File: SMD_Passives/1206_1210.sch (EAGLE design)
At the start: 4 parts

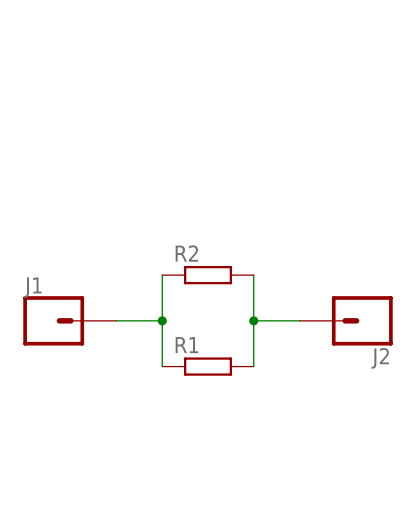
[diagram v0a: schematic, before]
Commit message: Updated passive SMD breakout boards to meet PCB specs
JLC PCB requires a 5x5mm minimum size, and the single SMD adapters were too small for this, so converted to make them wide enough, and made them "dual" to maximize the spaced used
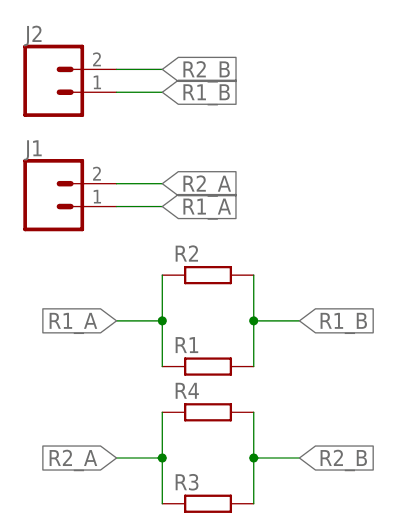
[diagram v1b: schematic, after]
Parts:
- added R3: (no value), bschulz_passives:R-EU_R1210
- added R4: (no value), bschulz_passives:R-EU_R1206
- J1, J2: device bschulz:CONN_01 -> bschulz:CONN_02
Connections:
- net N$1 renamed R1_A
- net N$2 renamed R1_B
- new net R2_A: J1.2, R3.1, R4.1
- new net R2_B: J2.2, R3.2, R4.2
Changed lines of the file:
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@@
 <part name="R1" library="bschulz_passives" deviceset="R-EU_" device="R1210"/>
 <part name="R2" library="bschulz_passives" deviceset="R-EU_" device="R1206"/>
-<part name="J1" library="bschulz" deviceset="CONN_01" device="" package3d_urn="urn:adsk.eagle:package:38028/1"/>
-<part name="J2" library="bschulz" deviceset="CONN_01" device="" package3d_urn="urn:adsk.eagle:package:38028/1"/>
+<part name="J1" library="bschulz" deviceset="CONN_02" device=""/>
+<part name="J2" library="bschulz" deviceset="CONN_02" device=""/>
+<part name="R3" library="bschulz_passives" deviceset="R-EU_" device="R1210"/>
+<part name="R4" library="bschulz_passives" deviceset="R-EU_" device="R1206"/>
 </parts>
 <sheets>
@@
 <attribute name="VALUE" x="21.59" y="14.478" size="1.778" layer="96"/>
 </instance>
-<instance part="J1" gate="G$1" x="7.62" y="12.7" smashed="yes">
-<attribute name="VALUE" x="5.08" y="7.874" size="1.778" layer="96" font="vector"/>
-<attribute name="NAME" x="5.08" y="15.748" size="1.778" layer="95" font="vector"/>
+<instance part="J1" gate="G$1" x="7.62" y="25.4" smashed="yes">
+<attribute name="VALUE" x="5.08" y="20.574" size="1.778" layer="96" font="vector"/>
+<attribute name="NAME" x="5.08" y="30.988" size="1.778" layer="95" font="vector"/>
 </instance>
-<instance part="J2" gate="G$1" x="43.18" y="12.7" smashed="yes" rot="R180">
-<attribute name="VALUE" x="45.72" y="17.526" size="1.778" layer="96" font="vector" rot="R180"/>
-<attribute name="NAME" x="45.72" y="9.652" size="1.778" layer="95" font="vector" rot="R180"/>
+<instance part="J2" gate="G$1" x="7.62" y="38.1" smashed="yes">
+<attribute name="VALUE" x="5.08" y="33.274" size="1.778" layer="96" font="vector"/>
+<attribute name="NAME" x="5.08" y="43.688" size="1.778" layer="95" font="vector"/>
+</instance>
+<instance part="R3" gate="G$1" x="25.4" y="-7.62" smashed="yes">
+<attribute name="NAME" x="21.59" y="-6.1214" size="1.778" layer="95"/>
+<attribute name="VALUE" x="21.59" y="-10.922" size="1.778" layer="96"/>
+</instance>
+<instance part="R4" gate="G$1" x="25.4" y="2.54" smashed="yes">
+<attribute name="NAME" x="21.59" y="4.0386" size="1.778" layer="95"/>
+<attribute name="VALUE" x="21.59" y="-0.762" size="1.778" layer="96"/>
 </instance>
 </instances>
@@
 </busses>
 <nets>
-<net name="N$1" class="0">
+<net name="R2_B" class="0">
+<segment>
+<pinref part="J2" gate="G$1" pin="2"/>
+<wire x1="15.24" y1="40.64" x2="20.32" y2="40.64" width="0.1524" layer="91"/>
+<label x="20.32" y="40.64" size="1.778" layer="95" xref="yes"/>
+</segment>
+<segment>
+<pinref part="R4" gate="G$1" pin="2"/>
+<pinref part="R3" gate="G$1" pin="2"/>
+<wire x1="30.48" y1="2.54" x2="30.48" y2="-2.54" width="0.1524" layer="91"/>
+<wire x1="30.48" y1="-2.54" x2="30.48" y2="-7.62" width="0.1524" layer="91"/>
+<wire x1="35.56" y1="-2.54" x2="30.48" y2="-2.54" width="0.1524" layer="91"/>
+<junction x="30.48" y="-2.54"/>
+<label x="35.56" y="-2.54" size="1.778" layer="95" xref="yes"/>
+</segment>
+</net>
+<net name="R1_B" class="0">
+<segment>
+<pinref part="J2" gate="G$1" pin="1"/>
+<wire x1="15.24" y1="38.1" x2="20.32" y2="38.1" width="0.1524" layer="91"/>
+<label x="20.32" y="38.1" size="1.778" layer="95" xref="yes"/>
+</segment>
+<segment>
+<pinref part="R2" gate="G$1" pin="2"/>
+<pinref part="R1" gate="G$1" pin="2"/>
+<wire x1="30.48" y1="17.78" x2="30.48" y2="12.7" width="0.1524" layer="91"/>
+<wire x1="30.48" y1="12.7" x2="30.48" y2="7.62" width="0.1524" layer="91"/>
+<wire x1="35.56" y1="12.7" x2="30.48" y2="12.7" width="0.1524" layer="91"/>
+<junction x="30.48" y="12.7"/>
+<label x="35.56" y="12.7" size="1.778" layer="95" xref="yes"/>
+</segment>
+</net>
+<net name="R2_A" class="0">
+<segment>
+<pinref part="J1" gate="G$1" pin="2"/>
+<wire x1="15.24" y1="27.94" x2="20.32" y2="27.94" width="0.1524" layer="91"/>
+<label x="20.32" y="27.94" size="1.778" layer="95" xref="yes"/>
+</segment>
+<segment>
+<pinref part="R3" gate="G$1" pin="1"/>
+<pinref part="R4" gate="G$1" pin="1"/>
+<wire x1="20.32" y1="-7.62" x2="20.32" y2="-2.54" width="0.1524" layer="91"/>
+<wire x1="20.32" y1="-2.54" x2="20.32" y2="2.54" width="0.1524" layer="91"/>
+<wire x1="15.24" y1="-2.54" x2="20.32" y2="-2.54" width="0.1524" layer="91"/>
+<junction x="20.32" y="-2.54"/>
+<label x="15.24" y="-2.54" size="1.778" layer="95" rot="R180" xref="yes"/>
+</segment>
+</net>
+<net name="R1_A" class="0">
+<segment>
+<pinref part="J1" gate="G$1" pin="1"/>
+<wire x1="15.24" y1="25.4" x2="20.32" y2="25.4" width="0.1524" layer="91"/>
+<label x="20.32" y="25.4" size="1.778" layer="95" xref="yes"/>
+</segment>
 <segment>
 <pinref part="R1" gate="G$1" pin="1"/>
 <pinref part="R2" gate="G$1" pin="1"/>
 <wire x1="20.32" y1="7.62" x2="20.32" y2="12.7" width="0.1524" layer="91"/>
-<pinref part="J1" gate="G$1" pin="1"/>
 <wire x1="20.32" y1="12.7" x2="20.32" y2="17.78" width="0.1524" layer="91"/>
 <wire x1="15.24" y1="12.7" x2="20.32" y2="12.7" width="0.1524" layer="91"/>
 <junction x="20.32" y="12.7"/>
-</segment>
-</net>
-<net name="N$2" class="0">
-<segment>
-<pinref part="R2" gate="G$1" pin="2"/>
-<pinref part="R1" gate="G$1" pin="2"/>
-<wire x1="30.48" y1="17.78" x2="30.48" y2="12.7" width="0.1524" layer="91"/>
-<pinref part="J2" gate="G$1" pin="1"/>
-<wire x1="30.48" y1="12.7" x2="30.48" y2="7.62" width="0.1524" layer="91"/>
-<wire x1="35.56" y1="12.7" x2="30.48" y2="12.7" width="0.1524" layer="91"/>
-<junction x="30.48" y="12.7"/>
+<label x="15.24" y="12.7" size="1.778" layer="95" rot="R180" xref="yes"/>
 </segment>
 </net>
@@
 </schematic>
 </drawing>
-<compatibility>
-<note version="8.3" severity="warning">
-Since Version 8.3, EAGLE supports URNs for individual library
-assets (packages, symbols, and devices). The URNs of those assets
-will not be understood (or retained) with this version.
-</note>
-<note version="8.3" severity="warning">
-Since Version 8.3, EAGLE supports the association of 3D packages
-with devices in libraries, schematics, and board files. Those 3D
-packages will not be understood (or retained) with this version.
-</note>
-</compatibility>
 </eagle>
